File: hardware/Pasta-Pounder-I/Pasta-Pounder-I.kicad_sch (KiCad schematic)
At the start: 62 parts, among them CN1 XT30UPB-M, CN2 B4B-PH-K-S(LF)(SN), J1 USB_C_Receptacle, J2 Brushed_Motor_1, J3 Brushed_Motor_2, J4 ESC_Port, J5 Flipper_port, J6 ESC_Terminal, Q1 AO3401A, SW1 RESET-SW, SW2 BOOT-SW, SW3 5.8 ZSPT, U1 DRV8874PWPR, U2 DRV8874PWPR, U4 USBLC6-2P6, U5 ESP32S3W1, U6 SY8113BADC, U7 SY8113BADC

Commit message: Fixed minor issues for schematic freeze
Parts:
- removed CN2: B4B-PH-K-S(LF)(SN), lcsc_footprints:C131334_CONN-TH_B4B-PH-K-S, symbol lcsc_imported:B4B-PH-K-S(LF)(SN)
- removed J5: Flipper_port, symbol Connector_Generic:Conn_01x03
- added C14: 220uF, symbol Device:C_Polarized
- added J5: JST-SH, symbol Connector_Generic:Conn_01x04
- C13: value C_Polarized -> 220uF
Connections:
- net GND: now also C14.2, J5.2 (Pin_2)
- net UART_RX: now also J5.3 (Pin_3)
- net UART_TX: now also J5.4 (Pin_4)
- net VCC: now also C14.1, J5.1 (Pin_1)
- net FLIPPER_PWM: no longer names the net of U5.22 (IO14)
- no-connect marks 33 -> 34
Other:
- moved on the sheet: J4, J6

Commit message: Removed old 5V buck converter
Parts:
- removed C20: 10uF,25V, PCM_JLCPCB:C_0603, symbol Device:C
- removed C21: 100nF, PCM_JLCPCB:C_0402, symbol Device:C
- removed C22: 10pF, PCM_JLCPCB:C_0402, symbol Device:C
- removed C23: 10uF, PCM_JLCPCB:C_0603, symbol Device:C
- removed L2: 4.7uH, lcsc_footprints:C98354_IND-SMD_L2_5-W2_0_WPN252012H, symbol Device:L
- removed R14: 36kΩ, PCM_JLCPCB:R_0402, symbol Device:R
- removed R15: 4k7Ω, PCM_JLCPCB:R_0402, symbol Device:R
- removed U6: SY8113BADC, lcsc_footprints:C78989_TSOT-23-6_L2_9-W1_6-P0_95-LS2_8-BR, symbol lcsc_imported:SY8113BADC
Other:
- note added: "Board Documentation"
- note removed: "5V Buck Converter"
- note removed: "Extra Robot Information"
- moved on the sheet: C26, C27, C28, C29, L3, R12, R13, U7

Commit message: Binded symbols to footprints; layout initial work
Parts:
- removed C12, C8: 470µF, symbol Device:C
- added C12, C8: 470uF, Capacitor_SMD:CP_Elec_6.3x7.7, symbol Device:C_Polarized
- C1, C10, C11, C2, C3, C4, C5, C6, C7, C9: footprint (none) -> PCM_JLCPCB:C_0603
- C13, C14: footprint (none) -> Capacitor_SMD:CP_Elec_6.3x7.7
- D1: footprint Diode_THT:D_DO-41_SOD81_P10.16mm_Horizontal -> Diode_SMD:D_SOD-323
- D3, D4: footprint (none) -> PCM_JLCPCB:D_0603
- J1: footprint (none) -> lcsc_footprints:C165948_USB-C_SMD-TYPE-C-31-M-12_1
- J2, J3, J6: footprint (none) -> lcsc_footprints:C8404_CONN-TH_WJ126V-5_0-2P
- J4: footprint (none) -> Connector_PinHeader_2.54mm:PinHeader_1x03_P2.54mm_Vertical
- J5: footprint (none) -> Connector_JST:JST_SH_BM04B-SRSS-TB_1x04-1MP_P1.00mm_Vertical
- Q1: footprint Package_TO_SOT_SMD:SOT-23 -> PCM_JLCPCB:Q_SOT-23
- R1, R10, R16, R17, R2, R3, R4, R5, R6, R7, R8, R9: footprint (none) -> PCM_JLCPCB:R_0603
- R11: value R -> 10KΩ; footprint (none) -> PCM_JLCPCB:R_0603
- R12, R13: footprint PCM_JLCPCB:R_0402 -> PCM_JLCPCB:R_0603
- SW1, SW2: footprint (none) -> lcsc_footprints:C115357_SW-SMD_L3_9-W3_0-P4_45
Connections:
- net GND: now also C12.2, C8.2
- net VCC: now also C12.1, C8.1

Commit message: Initial PCB Movements
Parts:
- U5: footprint RF_Module:ESP32-S3-WROOM-1 -> lcsc_footprints:C3013946_WIRELM-SMD_ESP32-S3-WROOM-1U
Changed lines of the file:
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@@
 			)
 		)
-		(property "Footprint" "RF_Module:ESP32-S3-WROOM-1"
+		(property "Footprint" "lcsc_footprints:C3013946_WIRELM-SMD_ESP32-S3-WROOM-1U"
 			(at 52.07 66.04 0)
 			(hide yes)

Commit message: idk what i even did but github showi ng changes
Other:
- company: Team Carbonara -> Carbonara Individuals
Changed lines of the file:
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@@
 		(title "Pasta Pounder I")
 		(rev "v1.0")
-		(company "Team Carbonara")
+		(company "Carbonara Individuals")
 		(comment 1 "Developed By: Daniel Principe & Saurya Shrestha")
 	)

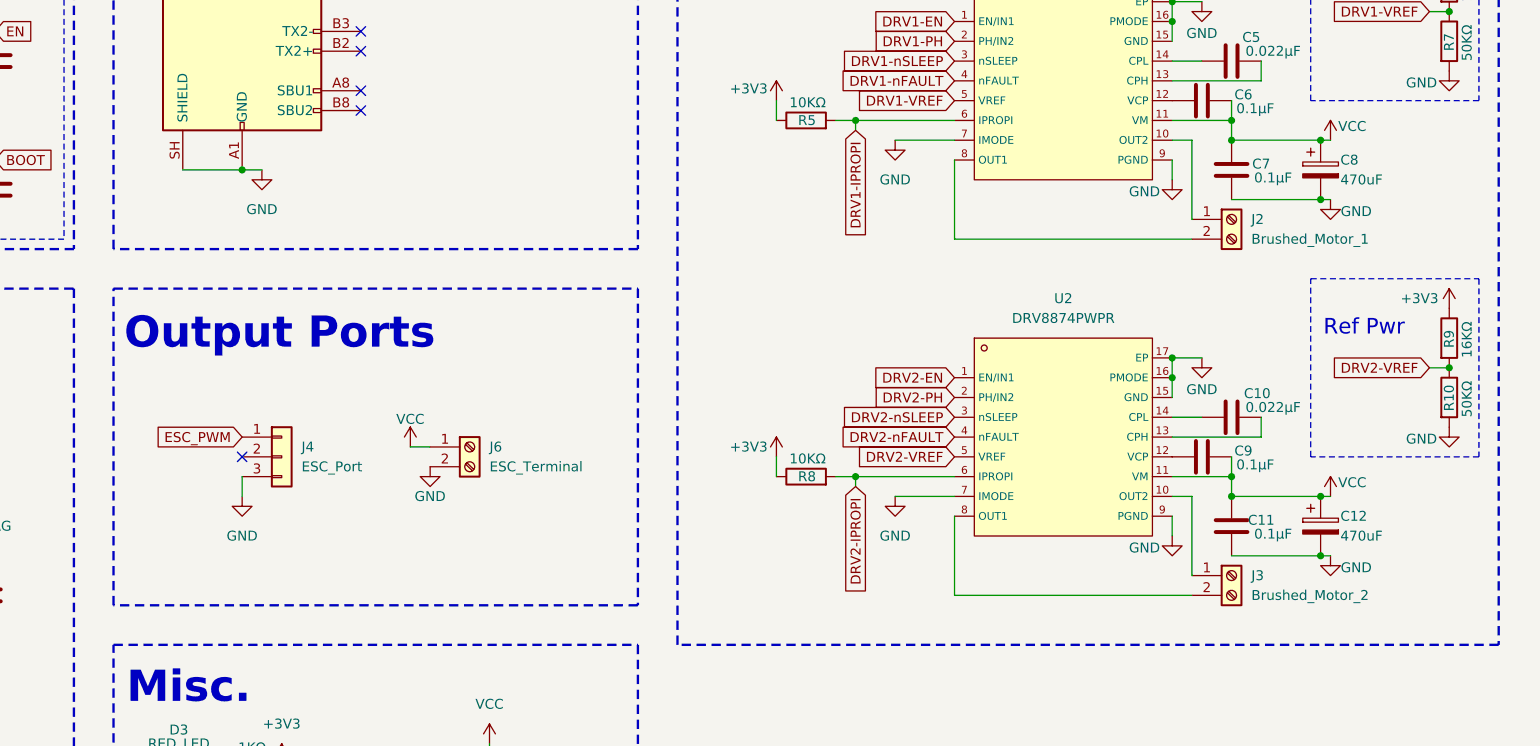
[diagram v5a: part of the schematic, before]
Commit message: Swapped terminals for solder pads
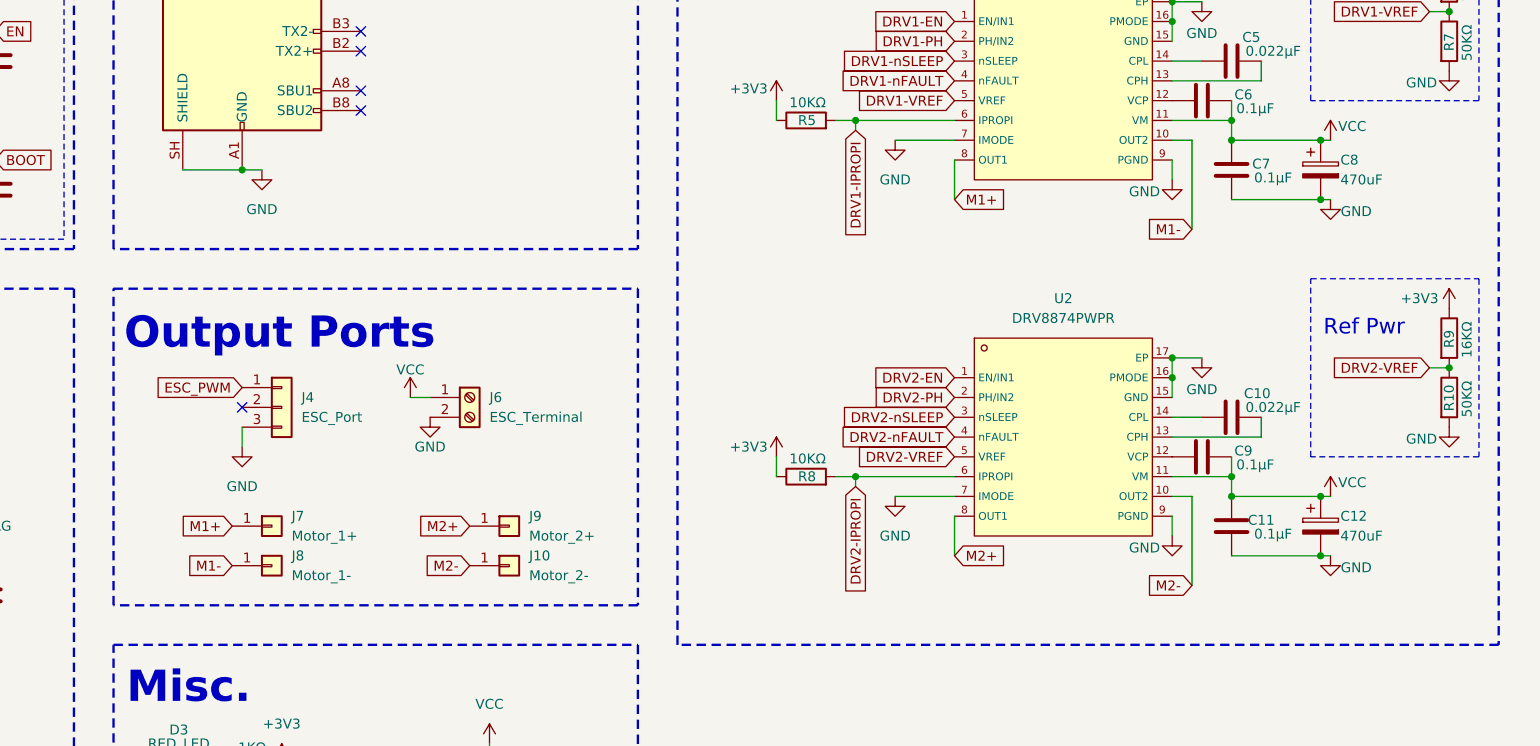
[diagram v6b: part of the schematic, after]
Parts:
- removed J2: Brushed_Motor_1, lcsc_footprints:C8404_CONN-TH_WJ126V-5_0-2P, symbol Connector:Screw_Terminal_01x02
- removed J3: Brushed_Motor_2, lcsc_footprints:C8404_CONN-TH_WJ126V-5_0-2P, symbol Connector:Screw_Terminal_01x02
- added J10: Motor_2-, Connector_Wire:SolderWirePad_1x01_SMD_2x4mm, symbol Connector_Generic:Conn_01x01
- added J7: Motor_1+, Connector_Wire:SolderWirePad_1x01_SMD_2x4mm, symbol Connector_Generic:Conn_01x01
- added J8: Motor_1-, Connector_Wire:SolderWirePad_1x01_SMD_2x4mm, symbol Connector_Generic:Conn_01x01
- added J9: Motor_2+, Connector_Wire:SolderWirePad_1x01_SMD_2x4mm, symbol Connector_Generic:Conn_01x01
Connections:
- net M1-: now reaches U1.10 (OUT2)
- net M1-: now also J8.1 (Pin_1)
- net M1+: now reaches U1.8 (OUT1)
- net M1+: now also J7.1 (Pin_1)
- net M2-: now reaches U2.10 (OUT2)
- net M2-: now also J10.1 (Pin_1)
- net M2+: now reaches U2.8 (OUT1)
- net M2+: now also J9.1 (Pin_1)
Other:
- moved on the sheet: J4, J6

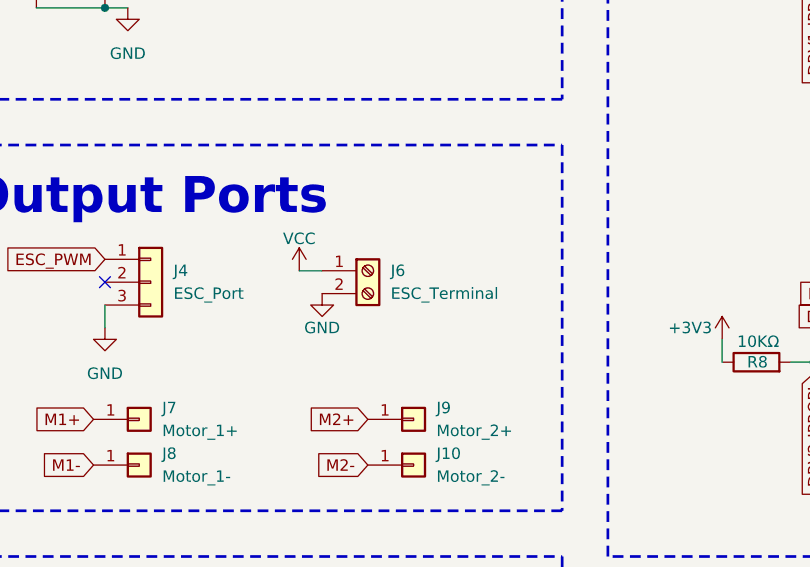
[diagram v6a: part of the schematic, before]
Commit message: Resized board to 70x25mm
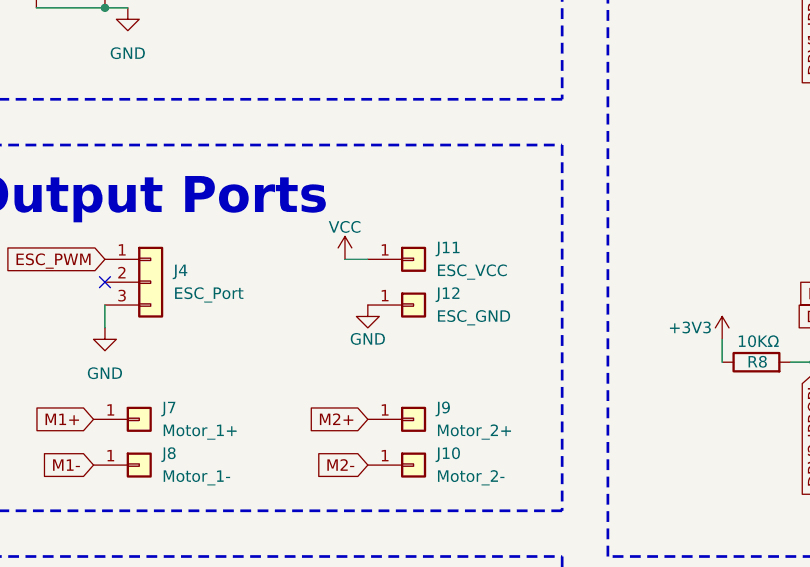
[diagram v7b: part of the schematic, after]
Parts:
- removed J6: ESC_Terminal, lcsc_footprints:C8404_CONN-TH_WJ126V-5_0-2P, symbol Connector:Screw_Terminal_01x02
- added J11: ESC_VCC, Connector_Wire:SolderWirePad_1x01_SMD_2x4mm, symbol Connector_Generic:Conn_01x01
- added J12: ESC_GND, Connector_Wire:SolderWirePad_1x01_SMD_2x4mm, symbol Connector_Generic:Conn_01x01
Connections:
- net GND: now also J12.1 (Pin_1)
- net VCC: now also J11.1 (Pin_1)
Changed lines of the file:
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@@
 	(wire
 		(pts
-			(xy 142.24 130.81) (xy 144.78 130.81)
+			(xy 147.32 129.54) (xy 149.86 129.54)
 		)
 		(stroke
@@
 	)
 	(symbol
-		(lib_id "Connector:Screw_Terminal_01x02")
-		(at 149.86 130.81 0)
-		(unit 1)
-		(body_style 1)
-		(exclude_from_sim no)
-		(in_bom yes)
-		(on_board yes)
-		(in_pos_files yes)
-		(dnp no)
-		(fields_autoplaced yes)
-		(property "Reference" "J6"
-			(at 152.4 130.8099 0)
-			(show_name no)
-			(do_not_autoplace no)
-			(effects
-				(font
-					(size 1.27 1.27)
-				)
-				(justify left)
-			)
-		)
-		(property "Value" "ESC_Terminal"
-			(at 152.4 133.3499 0)
-			(show_name no)
-			(do_not_autoplace no)
-			(effects
-				(font
-					(size 1.27 1.27)
-				)
-				(justify left)
-			)
-		)
-		(property "Footprint" "lcsc_footprints:C8404_CONN-TH_WJ126V-5_0-2P"
-			(at 149.86 130.81 0)
-			(hide yes)
-			(show_name no)
-			(do_not_autoplace no)
-			(effects
-				(font
-					(size 1.27 1.27)
-				)
-			)
-		)
-		(property "Datasheet" ""
-			(at 149.86 130.81 0)
-			(hide yes)
-			(show_name no)
-			(do_not_autoplace no)
-			(effects
-				(font
-					(size 1.27 1.27)
-				)
-			)
-		)
-		(property "Description" "Generic screw terminal, single row, 01x02, script generated (kicad-library-utils/schlib/autogen/connector/)"
-			(at 149.86 130.81 0)
-			(hide yes)
-			(show_name no)
-			(do_not_autoplace no)
-			(effects
-				(font
-					(size 1.27 1.27)
-				)
-			)
-		)
-		(pin "2"
-		)
-		(pin "1"
-		)
-		(instances
-			(project "Pasta-Pounder-I"
-				(path "/4b2b0ba2-7cf9-4aa2-924c-d1661524830e"
-					(reference "J6")
-					(unit 1)
-				)
-			)
-		)
-	)
-	(symbol
 		(lib_id "power:+3V3")
 		(at 275.59 119.38 0)
@@
 	(symbol
 		(lib_id "power:GND")
-		(at 144.78 133.35 0)
+		(at 149.86 134.62 0)
 		(unit 1)
 		(body_style 1)
@@
 		(dnp no)
 		(property "Reference" "#PWR037"
-			(at 144.78 139.7 0)
+			(at 149.86 140.97 0)
 			(hide yes)
 			(show_name no)
@@
 		)
 		(property "Value" "GND"
-			(at 144.78 137.16 0)
+			(at 149.86 138.43 0)
 			(show_name no)
 			(do_not_autoplace no)
@@
 		)
 		(property "Footprint" ""
-			(at 144.78 133.35 0)
+			(at 149.86 134.62 0)
 			(hide yes)
 			(show_name no)
@@
 		)
 		(property "Datasheet" ""
-			(at 144.78 133.35 0)
+			(at 149.86 134.62 0)
 			(hide yes)
 			(show_name no)
@@
 		)
 		(property "Description" "Power symbol creates a global label with name \"GND\" , ground"
-			(at 144.78 133.35 0)
+			(at 149.86 134.62 0)
 			(hide yes)
 			(show_name no)
@@
 	(symbol
 		(lib_id "power:VCC")
-		(at 142.24 130.81 0)
+		(at 147.32 129.54 0)
 		(unit 1)
 		(body_style 1)
@@
 		(dnp no)
 		(property "Reference" "#PWR031"
-			(at 142.24 134.62 0)
+			(at 147.32 133.35 0)
 			(hide yes)
 			(show_name no)
@@
 		)
 		(property "Value" "VCC"
-			(at 142.24 127.254 0)
+			(at 147.32 125.984 0)
 			(show_name no)
 			(do_not_autoplace no)
@@
 		)
 		(property "Footprint" ""
-			(at 142.24 130.81 0)
+			(at 147.32 129.54 0)
 			(hide yes)
 			(show_name no)
@@
 		)
 		(property "Datasheet" ""
-			(at 142.24 130.81 0)
+			(at 147.32 129.54 0)
 			(hide yes)
 			(show_name no)
@@
 		)
 		(property "Description" "Power symbol creates a global label with name \"VCC\""
-			(at 142.24 130.81 0)
+			(at 147.32 129.54 0)
 			(hide yes)
 			(show_name no)
@@
 	)
 	(symbol
+		(lib_id "Connector_Generic:Conn_01x01")
+		(at 154.94 129.54 0)
+		(unit 1)
+		(body_style 1)
+		(exclude_from_sim no)
+		(in_bom yes)
+		(on_board yes)
+		(in_pos_files yes)
+		(dnp no)
+		(fields_autoplaced yes)
+		(property "Reference" "J11"
+			(at 157.48 128.2699 0)
+			(show_name no)
+			(do_not_autoplace no)
+			(effects
+				(font
+					(size 1.27 1.27)
+				)
+				(justify left)
+			)
+		)
+		(property "Value" "ESC_VCC"
+			(at 157.48 130.8099 0)
+			(show_name no)
+			(do_not_autoplace no)
+			(effects
+				(font
+					(size 1.27 1.27)
+				)
+				(justify left)
+			)
+		)
+		(property "Footprint" "Connector_Wire:SolderWirePad_1x01_SMD_2x4mm"
+			(at 154.94 129.54 0)
+			(hide yes)
+			(show_name no)
+			(do_not_autoplace no)
+			(effects
+				(font
+					(size 1.27 1.27)
+				)
+			)
+		)
+		(property "Datasheet" ""
+			(at 154.94 129.54 0)
+			(hide yes)
+			(show_name no)
+			(do_not_autoplace no)
+			(effects
+				(font
+					(size 1.27 1.27)
+				)
+			)
+		)
+		(property "Description" "Generic connector, single row, 01x01, script generated (kicad-library-utils/schlib/autogen/connector/)"
+			(at 154.94 129.54 0)
+			(hide yes)
+			(show_name no)
+			(do_not_autoplace no)
+			(effects
+				(font
+					(size 1.27 1.27)
+				)
+			)
+		)
+		(pin "1"
+		)
+		(instances
+			(project "Pasta-Pounder-I"
+				(path "/4b2b0ba2-7cf9-4aa2-924c-d1661524830e"
+					(reference "J11")
+					(unit 1)
+				)
+			)
+		)
+	)
+	(symbol
 		(lib_id "Device:R")
 		(at 30.48 40.64 180)
@@
 					(unit 1)
 				)
+			)
+		)
+	)
+	(symbol
+		(lib_id "Connector_Generic:Conn_01x01")
+		(at 154.94 134.62 0)
+		(unit 1)
+		(body_style 1)
+		(exclude_from_sim no)
+		(in_bom yes)
+		(on_board yes)
+		(in_pos_files yes)
+		(dnp no)
+		(fields_autoplaced yes)
+		(property "Reference" "J12"
+			(at 157.48 133.3499 0)
+			(show_name no)
+			(do_not_autoplace no)
+			(effects
+				(font
+					(size 1.27 1.27)
+				)
+				(justify left)
+			)
+		)
+		(property "Value" "ESC_GND"
+			(at 157.48 135.8899 0)
+			(show_name no)
+			(do_not_autoplace no)
+			(effects
+				(font
+					(size 1.27 1.27)
+				)
+				(justify left)
+			)
+		)
+		(property "Footprint" "Connector_Wire:SolderWirePad_1x01_SMD_2x4mm"
+			(at 154.94 134.62 0)
+			(hide yes)
+			(show_name no)
+			(do_not_autoplace no)
+			(effects
+				(font
+					(size 1.27 1.27)
+				)
+			)
+		)
+		(property "Datasheet" ""
+			(at 154.94 134.62 0)
+			(hide yes)
+			(show_name no)
+			(do_not_autoplace no)
+			(effects
+				(font
+					(size 1.27 1.27)
+				)
+			)
+		)
+		(property "Description" "Generic connector, single row, 01x01, script generated (kicad-library-utils/schlib/autogen/connector/)"
+			(at 154.94 134.62 0)
+			(hide yes)
+			(show_name no)
+			(do_not_autoplace no)
+			(effects
+				(font
+					(size 1.27 1.27)
+				)
+			)
+		)
+		(pin "1"
+		)
+		(instances
+			(project "Pasta-Pounder-I"
+				(path "/4b2b0ba2-7cf9-4aa2-924c-d1661524830e"
+					(reference "J12")
+					(unit 1)
+				)

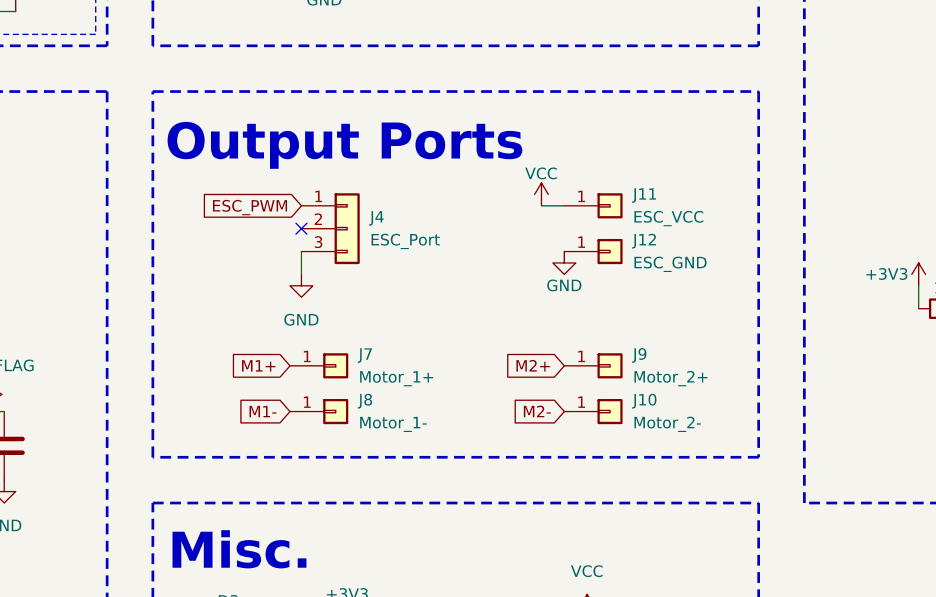
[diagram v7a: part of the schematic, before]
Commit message: L Shaped Initial Movements
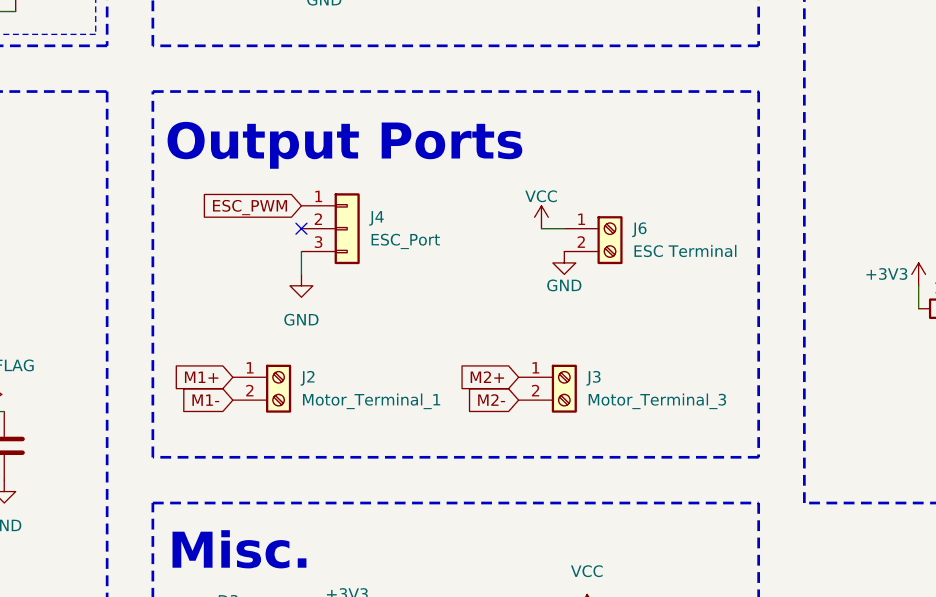
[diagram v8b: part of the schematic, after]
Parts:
- removed J10: Motor_2-, Connector_Wire:SolderWirePad_1x01_SMD_2x4mm, symbol Connector_Generic:Conn_01x01
- removed J11: ESC_VCC, Connector_Wire:SolderWirePad_1x01_SMD_2x4mm, symbol Connector_Generic:Conn_01x01
- removed J12: ESC_GND, Connector_Wire:SolderWirePad_1x01_SMD_2x4mm, symbol Connector_Generic:Conn_01x01
- removed J7: Motor_1+, Connector_Wire:SolderWirePad_1x01_SMD_2x4mm, symbol Connector_Generic:Conn_01x01
- removed J8: Motor_1-, Connector_Wire:SolderWirePad_1x01_SMD_2x4mm, symbol Connector_Generic:Conn_01x01
- removed J9: Motor_2+, Connector_Wire:SolderWirePad_1x01_SMD_2x4mm, symbol Connector_Generic:Conn_01x01
- added J2: Motor_Terminal_1, lcsc_footprints:C8404_CONN-TH_WJ126V-5_0-2P, symbol Connector:Screw_Terminal_01x02
- added J3: Motor_Terminal_3, lcsc_footprints:C8404_CONN-TH_WJ126V-5_0-2P, symbol Connector:Screw_Terminal_01x02
- added J6: ESC Terminal, lcsc_footprints:C8404_CONN-TH_WJ126V-5_0-2P, symbol Connector:Screw_Terminal_01x02
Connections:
- net GND: now also J6.2 (Pin_2)
- net M1+: now also J2.1 (Pin_1)
- net M1-: now also J2.2 (Pin_2)
- net M2+: now also J3.1 (Pin_1)
- net M2-: now also J3.2 (Pin_2)
- net VCC: now also J6.1 (Pin_1)
